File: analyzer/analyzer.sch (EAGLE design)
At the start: 38 parts, among them J4 USBSMD, U1 ATA6631, U2 FT230X, U3 ATMEGA328P, U4 MOCD208M, X1 16MHz

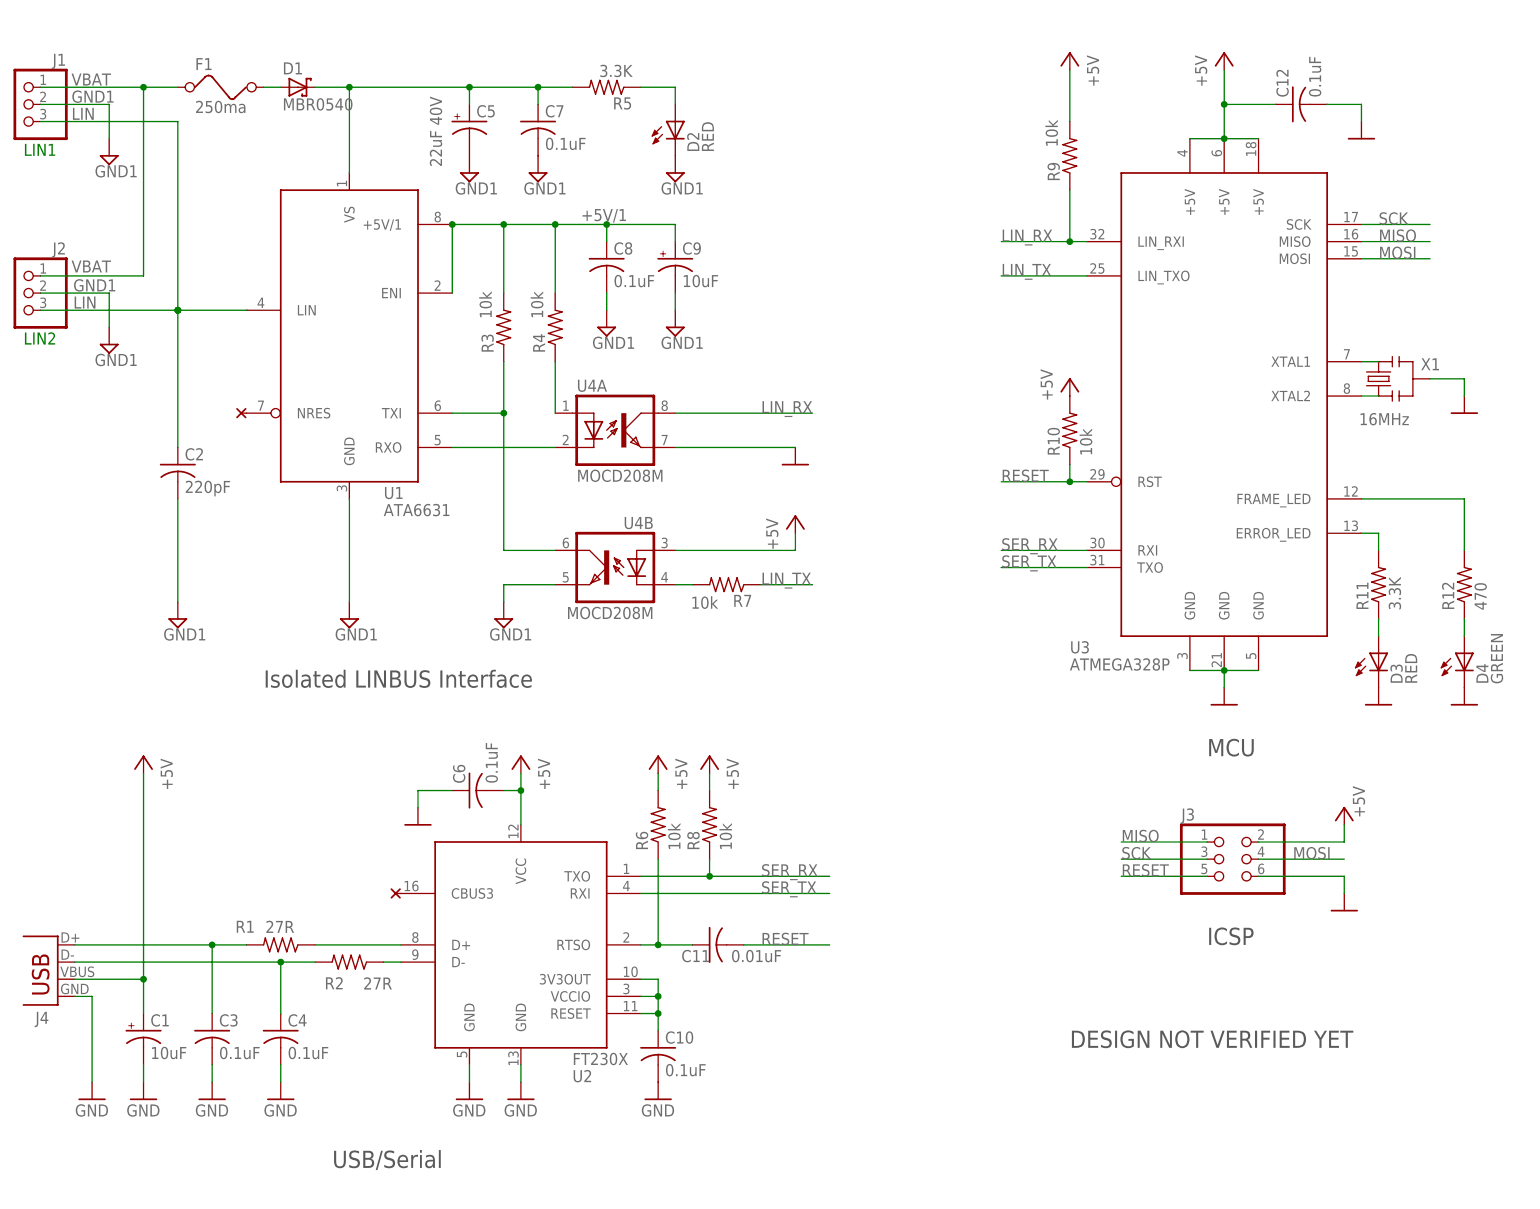
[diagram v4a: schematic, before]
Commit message: Added 3.3 to 5V level converter.
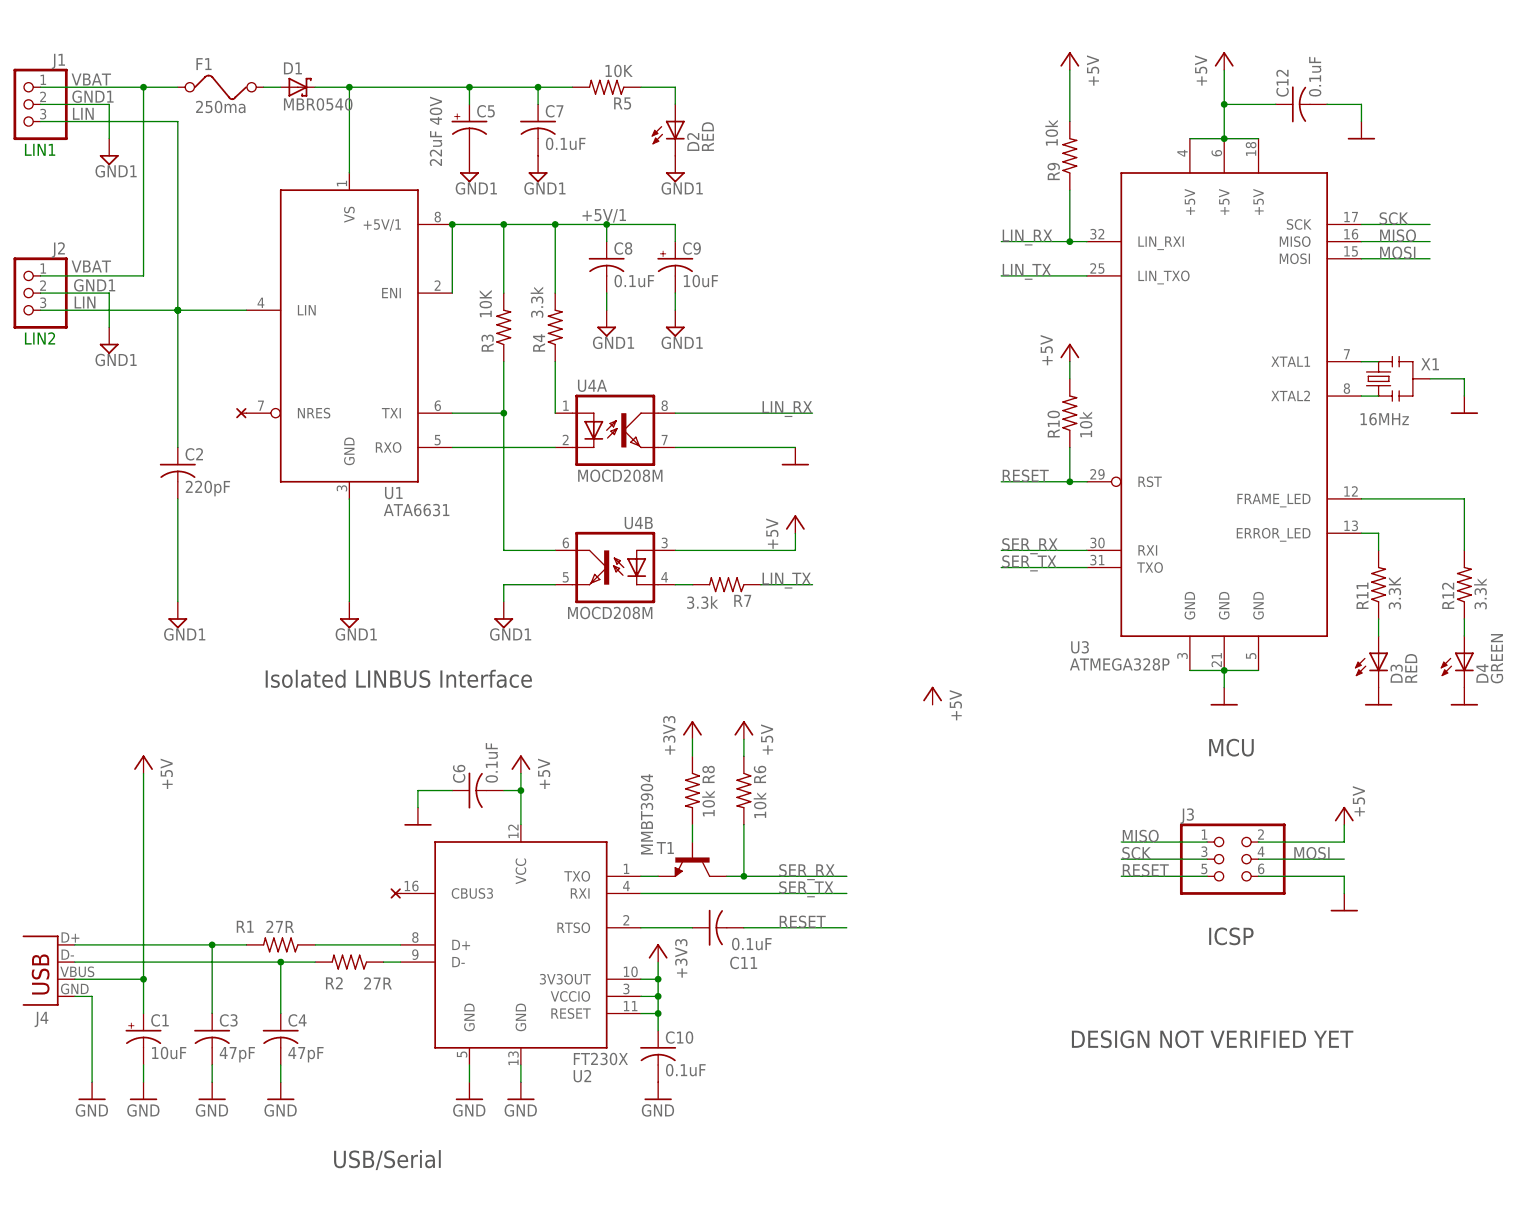
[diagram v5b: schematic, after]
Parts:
- added T1: MMBT3904, transistor:MMBT3904LT1-NPN-SOT23-BEC
- C11: value 0.01uF -> 0.1uF
- C3, C4: value 0.1uF -> 47pF
- R12: value 470 -> 3.3k
- R3: value 10k -> 10K
- R4, R7: value 10k -> 3.3k
- R5: value 3.3K -> 10K
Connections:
- removed net N$18: C10.1, U2.3V3OUT, U2.RESET, U2.VCCIO
- new net +3V3: C10.1, R8.1, U2.3V3OUT, U2.RESET, U2.VCCIO
- new net N$19: R8.2, T1.B
- new net N$2: T1.E, U2.TXO
- net +5V: now also R6.1; no longer R6.2, R8.2
- net N$20: no longer R6.1
- net SER_RX: now also R6.2, T1.C; no longer R8.1, U2.TXO
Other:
- moved on the sheet: C11, R10, R6, R8

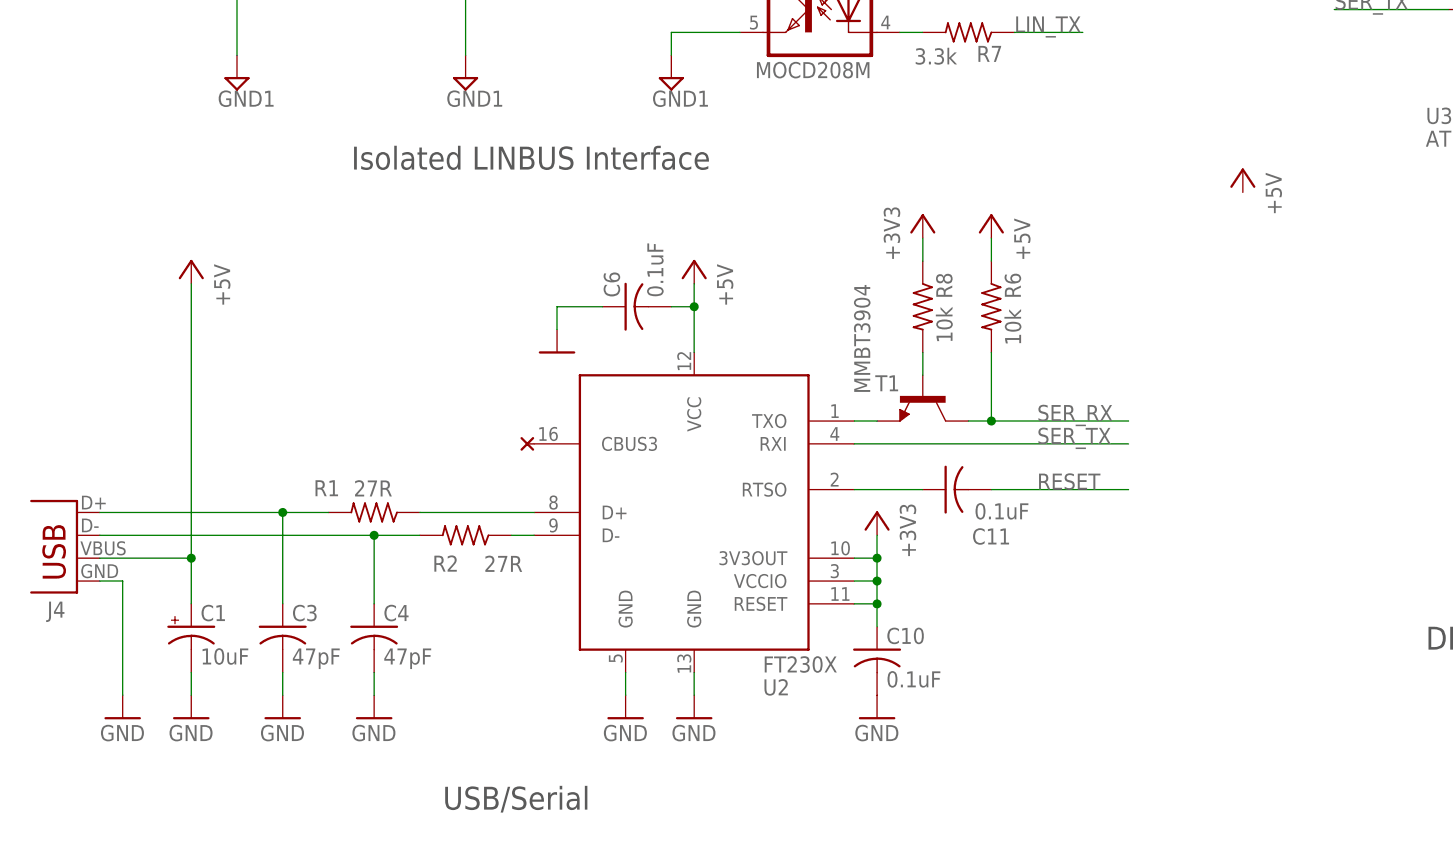
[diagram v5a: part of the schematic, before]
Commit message: Replaced the usb/serial chip to FT232RL. Larger but requires less glue components.
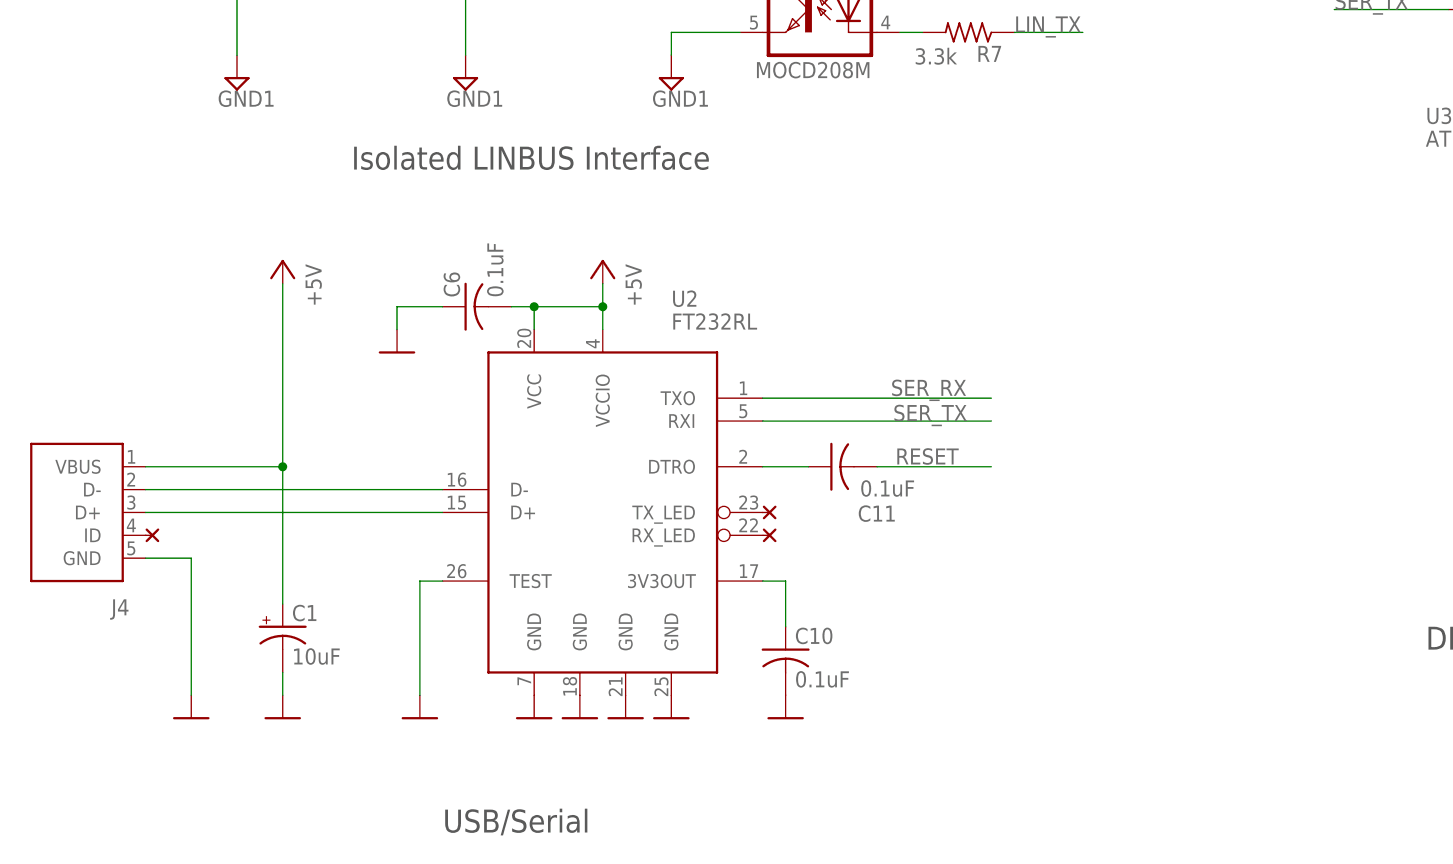
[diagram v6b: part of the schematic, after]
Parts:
- removed C3, C4: 47pF, rcl:C-USC0805
- removed R1, R2: 27R, rcl:R-US_R0805
- removed R6, R8: 10k, rcl:R-US_R0805
- removed T1: MMBT3904, transistor:MMBT3904LT1-NPN-SOT23-BEC
- U2: value FT230X -> FT232RL; device analyzer:FT230X -> analyzer:FT232RL
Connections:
- removed net +3V3: C10.1, R8.1, U2.3V3OUT, U2.RESET, U2.VCCIO
- removed net N$19: R8.2, T1.B
- removed net N$2: T1.E, U2.TXO
- removed net N$20: C11.1, U2.RTSO
- net +5V: now also U2.VCCIO; no longer R6.1
- net GND: now also U2.GND@3, U2.GND@4, U2.TEST; no longer C3.2, C4.2
- net N$10: now also U2.D+; no longer C3.1, R1.2
- net N$11: now also C11.1, U2.DTRO; no longer R1.1, U2.D+
- net N$15: now also U2.D-; no longer C4.1, R2.2
- net N$16: now also C10.1, U2.3V3OUT; no longer R2.1, U2.D-
- net SER_RX: now also U2.TXO; no longer R6.2, T1.C
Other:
- moved on the sheet: C1, C10, C11, C6
